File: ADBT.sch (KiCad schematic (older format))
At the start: 99 parts, among them J1 ADB1, J2 microUSB, Q1 AO3401, Q2 MMBT3904, Q3 MMBT3904, Q4 MMBT3904, Q5 MMBT3904, SW1 SW_Push, SW2 SW_Push, U1 ESP-WROOM-32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

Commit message: Add ground connection to LPseries mounting holes in schematic
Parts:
- H1, H2, H3, H4: symbol Mechanical:MountingHole -> Mechanical:MountingHole_Pad
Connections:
- net GND: now also H1.1, H2.1, H3.1, H4.1
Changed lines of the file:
@@
 encoding utf-8
 Sheet 1 1
-Title "RAM2E II"
-Date "2020-07-25"
-Rev "1.0"
+Title "ADBT"
+Date "2021-02-05"
+Rev "0.5"
 Comp "Garrett's Workshop"
 Comment1 ""
@@
 ESP32 module
 Wire Notes Line
-	2450 5850 1100 5850
-Text Notes 1250 5800 0    50   ~ 0
+	2450 5700 1100 5700
+Text Notes 1250 5650 0    50   ~ 0
 mounting holes & fiducials
 $Comp
@@
 	1100 6900 2450 6900
 Wire Notes Line
-	2450 5850 2450 6900
-Wire Notes Line
-	1100 5850 1100 6900
+	2450 5700 2450 6900
+Wire Notes Line
+	1100 5700 1100 6900
 Text Notes 2900 7100 0    50   ~ 0
 bypass capacitance
@@
 $EndComp
 $Comp
-L Mechanical:MountingHole H4
+L Mechanical:MountingHole_Pad H4
 U 1 1 5CC7E0C0
-P 2150 6000
-F 0 "H4" H 2250 6000 50  0000 L CNN
-F 1 " " H 2250 5960 50  0000 L CNN
-F 2 "stdpads:LPSeries-Screw" H 2150 6000 50  0001 C CNN
-F 3 "~" H 2150 6000 50  0001 C CNN
-	1    2150 6000
-	1    0    0    -1
-$EndComp
-$Comp
-L Mechanical:MountingHole H2
+P 2150 5900
+F 0 "H4" H 2250 5950 50  0000 L CNN
+F 1 " " H 2250 5860 50  0000 L CNN
+F 2 "stdpads:LPSeries-Screw" H 2150 5900 50  0001 C CNN
+F 3 "~" H 2150 5900 50  0001 C CNN
+	1    2150 5900
+	1    0    0    -1
+$EndComp
+$Comp
+L Mechanical:MountingHole_Pad H2
 U 1 1 5CC795A2
-P 1550 6000
-F 0 "H2" H 1650 6000 50  0000 L CNN
-F 1 " " H 1650 5960 50  0000 L CNN
-F 2 "stdpads:LPSeries-Screw" H 1550 6000 50  0001 C CNN
-F 3 "~" H 1550 6000 50  0001 C CNN
-	1    1550 6000
-	1    0    0    -1
-$EndComp
-$Comp
-L Mechanical:MountingHole H1
+P 1550 5900
+F 0 "H2" H 1650 5950 50  0000 L CNN
+F 1 " " H 1650 5860 50  0000 L CNN
+F 2 "stdpads:LPSeries-Screw" H 1550 5900 50  0001 C CNN
+F 3 "~" H 1550 5900 50  0001 C CNN
+	1    1550 5900
+	1    0    0    -1
+$EndComp
+$Comp
+L Mechanical:MountingHole_Pad H1
 U 1 1 5CC53461
-P 1250 6000
-F 0 "H1" H 1350 6000 50  0000 L CNN
-F 1 " " H 1350 5960 50  0000 L CNN
-F 2 "stdpads:LPSeries-Screw" H 1250 6000 50  0001 C CNN
-F 3 "~" H 1250 6000 50  0001 C CNN
-	1    1250 6000
-	1    0    0    -1
-$EndComp
-$Comp
-L Mechanical:MountingHole H3
+P 1250 5900
+F 0 "H1" H 1350 5950 50  0000 L CNN
+F 1 " " H 1350 5860 50  0000 L CNN
+F 2 "stdpads:LPSeries-Screw" H 1250 5900 50  0001 C CNN
+F 3 "~" H 1250 5900 50  0001 C CNN
+	1    1250 5900
+	1    0    0    -1
+$EndComp
+$Comp
+L Mechanical:MountingHole_Pad H3
 U 1 1 5CC7E0B9
-P 1850 6000
-F 0 "H3" H 1950 6000 50  0000 L CNN
-F 1 " " H 1950 5960 50  0000 L CNN
-F 2 "stdpads:LPSeries-Screw" H 1850 6000 50  0001 C CNN
-F 3 "~" H 1850 6000 50  0001 C CNN
-	1    1850 6000
+P 1850 5900
+F 0 "H3" H 1950 5950 50  0000 L CNN
+F 1 " " H 1950 5860 50  0000 L CNN
+F 2 "stdpads:LPSeries-Screw" H 1850 5900 50  0001 C CNN
+F 3 "~" H 1850 5900 50  0001 C CNN
+	1    1850 5900
 	1    0    0    -1
 $EndComp
@@
 $EndComp
 Connection ~ 900  1150
+Wire Wire Line
+	2150 6000 1850 6000
+Connection ~ 2150 6000
+Connection ~ 1550 6000
+Wire Wire Line
+	1550 6000 1250 6000
+Connection ~ 1850 6000
+Wire Wire Line
+	1850 6000 1550 6000
+Wire Wire Line
+	2150 6000 2250 5950
+$Comp
+L power:GND #PWR?
+U 1 1 602195C0
+P 2250 5950
+F 0 "#PWR?" H 2250 5700 50  0001 C CNN
+F 1 "GND" H 2250 5800 50  0000 C CNN
+F 2 "" H 2250 5950 50  0001 C CNN
+F 3 "" H 2250 5950 50  0001 C CNN
+	1    2250 5950
+	-1   0    0    -1
+$EndComp
 $EndSCHEMATC

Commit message: Switch to MLCC caps
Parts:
- removed C1, C2: 470u, stdpads:CP_Elec_10mm, symbol Device:CP_Small
- removed C27: 2u2, stdpads:C_0603, symbol Device:C_Small
- removed R18: 1k, stdpads:R_0603, symbol Device:R_Small
- removed SW2: SW_Push, stdpads:XKB_TS-1187A, symbol Switch:SW_Push
- added C1, C2: 100u, stdpads:C_1210, symbol Device:C_Small
- C11: value 100n -> 100u; footprint stdpads:C_0603 -> stdpads:C_1210
- C25, C26: value 2u2 -> 100u; footprint stdpads:C_0603 -> stdpads:C_1210
- R4: value 3k3 -> 1k
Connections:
- net +3V3: now also C11.1, C2.1
- net +5V: now also C1.1; no longer C11.1
- net BLED: now also U1.31 (IO19)
- net BTN0: now also U1.33 (IO21)
- net GLED: now also U1.30 (IO18)
- net GND: now also C11.2, C1.2, C2.2; no longer R4.2
- net RLED: now also U1.29 (IO5)
- net at D2.2 (A), F2.2, R2.2: now also R4.1
- net at C12.1, D6.1 (K), Q1.1 (G)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: no longer C11.2, R4.1
- no-connect marks 15 -> 18
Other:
- moved on the sheet: C18, C19, C20, C21, C22, C23, C24, R4

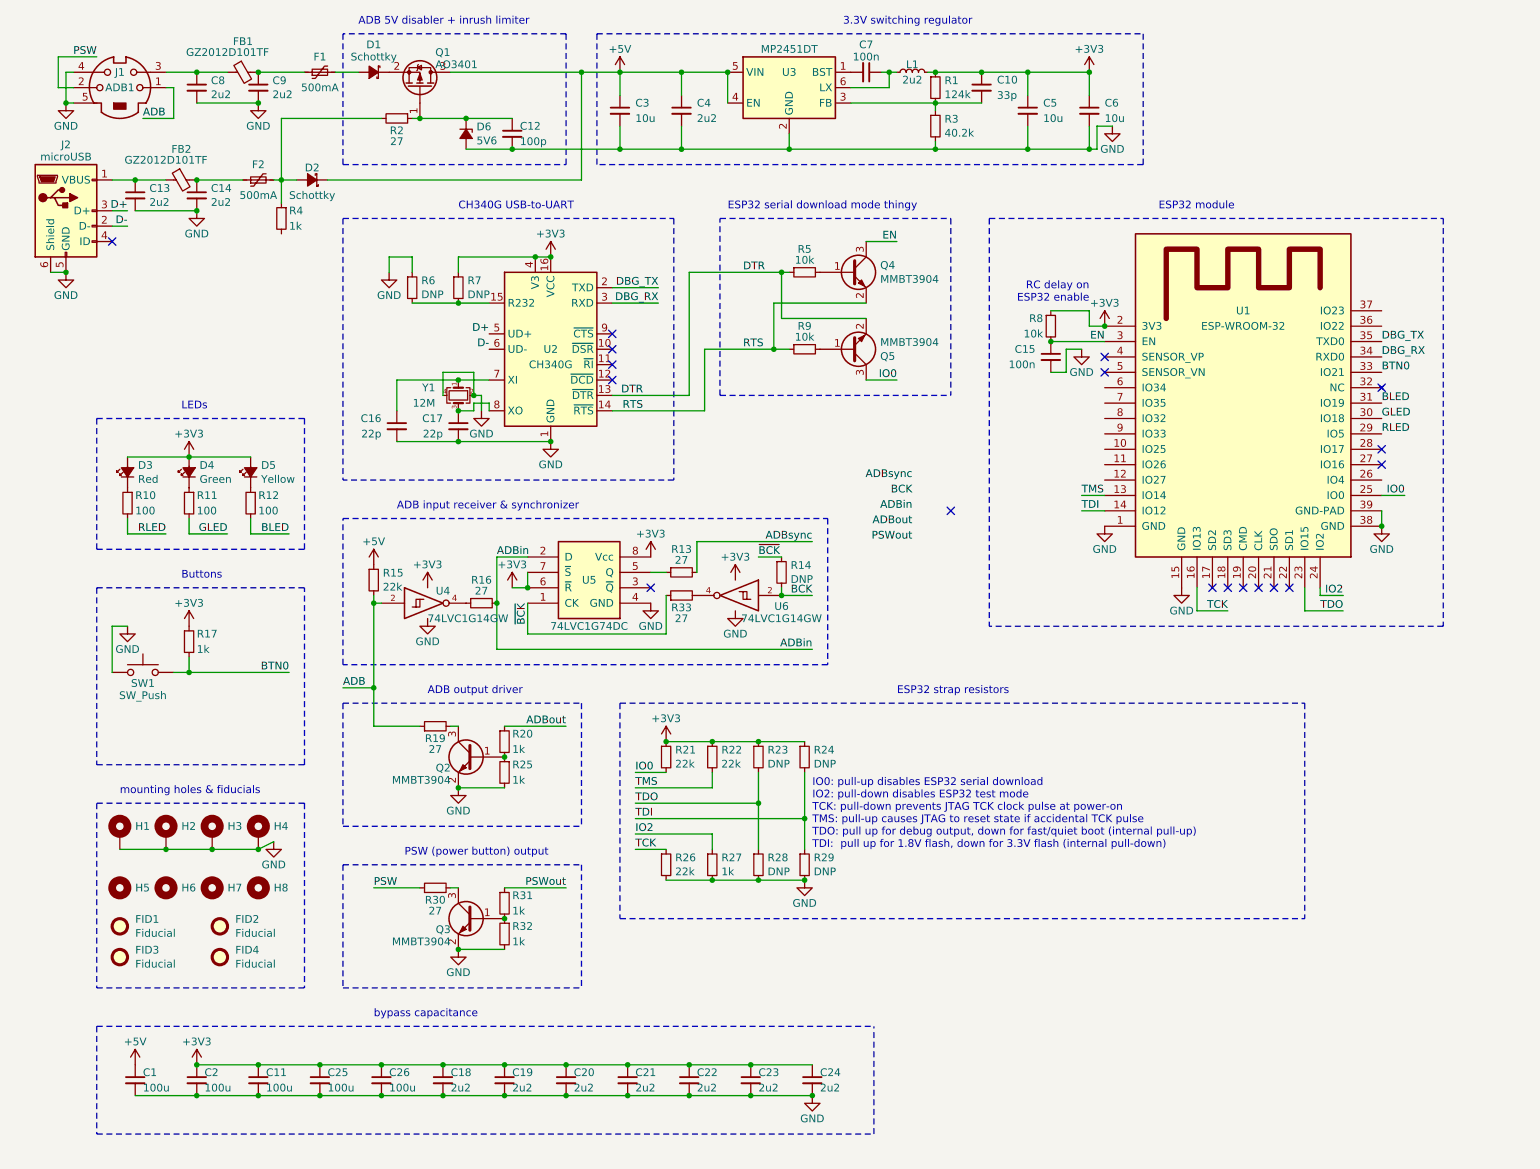
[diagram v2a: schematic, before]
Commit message: Lay out most of board
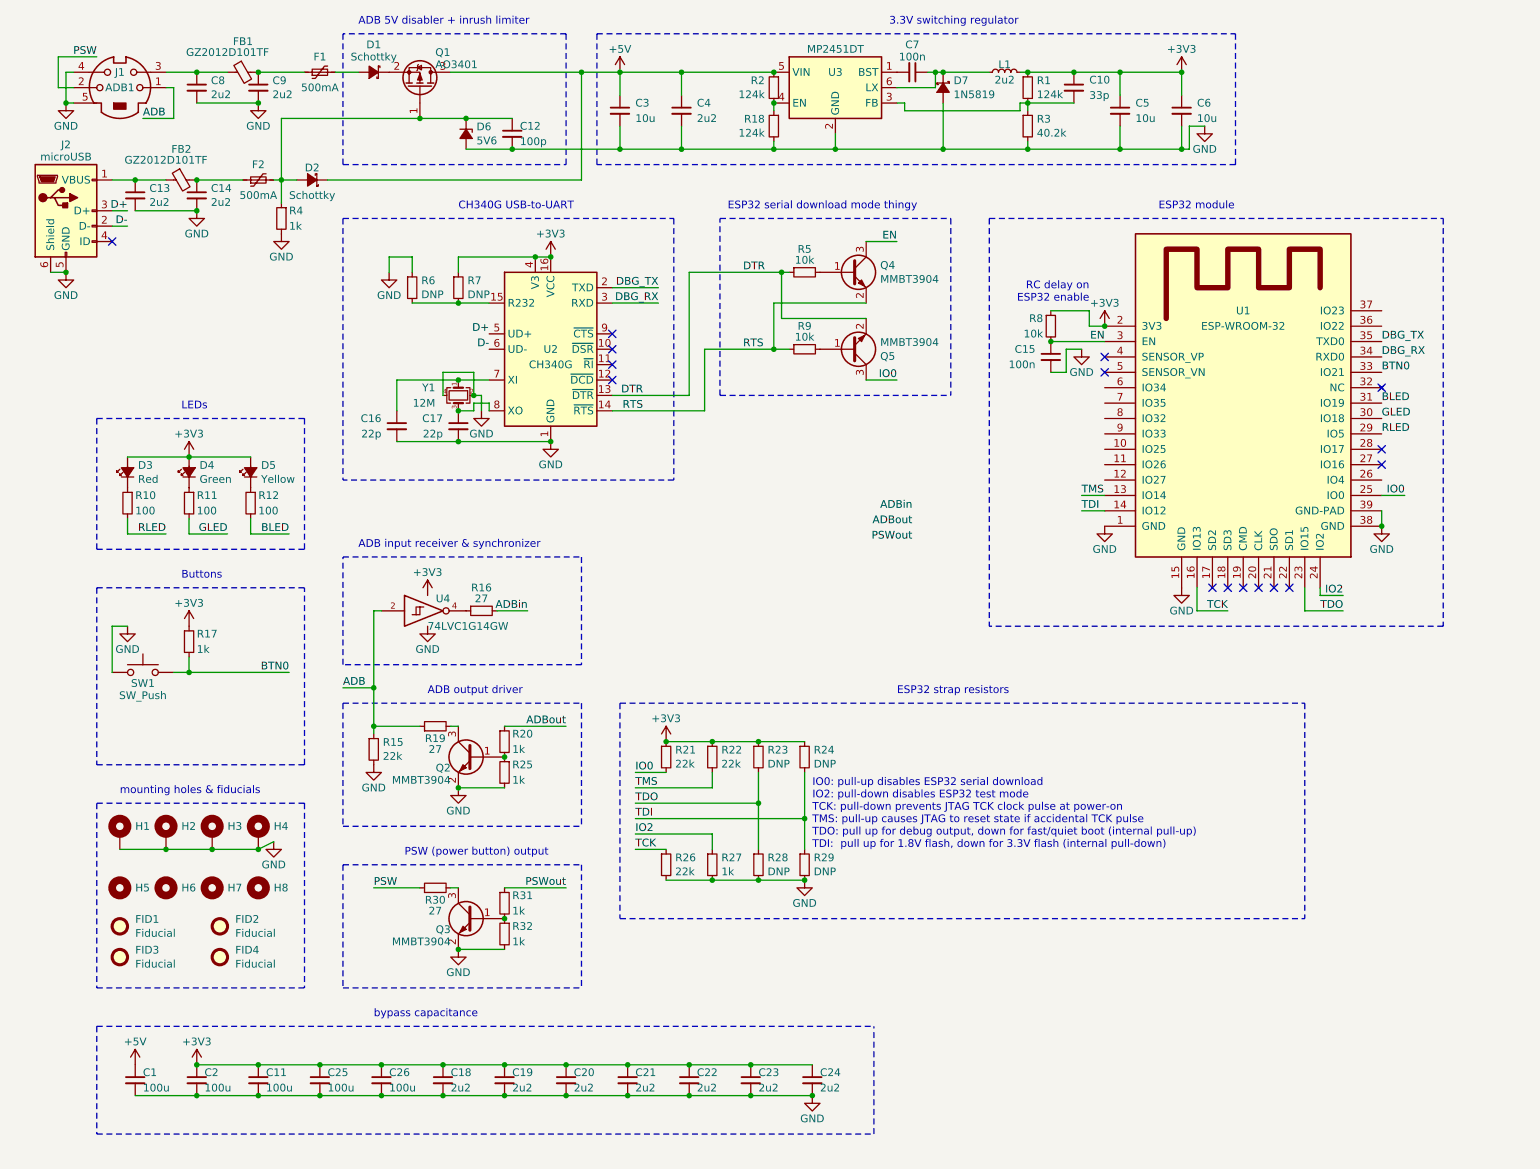
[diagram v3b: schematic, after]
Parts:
- removed R13, R33: 27, stdpads:R_0603, symbol Device:R_Small
- removed R14: DNP, stdpads:R_0603, symbol Device:R_Small
- removed U5: 74LVC1G74DC, stdpads:NXP_VSSOP-8_2.3x2mm, symbol GW_Logic:741G74DC
- removed U6: 74LVC1G14GW, stdpads:SOT-353, symbol 74xGxx:74LVC1G14
- added D7: 1N5819, stdpads:D_SOD-123, symbol Device:D_Schottky_Small_ALT
- added R18: 124k, stdpads:R_0603, symbol Device:R_Small
- R2: value 27 -> 124k
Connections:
- net +5V: now also R2.1; no longer R15.1, U3.4 (EN)
- net ADB: now also R15.1; no longer R15.2
- net GND: now also R15.2, R4.2, D7.2 (A), R18.2
- net at C7.1, L1.1, U3.6 (LX): now also D7.1 (K)
- net at D2.2 (A), F2.2, R4.1: now also C12.1, D6.1 (K), Q1.1 (G); no longer R2.2
- new net: R18.1, R2.2, U3.4 (EN)
- no-connect marks 18 -> 16
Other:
- moved on the sheet: C10, C5, C6, C7, L1, R1, R15, R16, R3, U3, U4

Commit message: Stitch board around edges
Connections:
- net at C16.1, U2.7 (XI): now also Y1.3; no longer Y1.1
- net at C17.1, U2.8 (XO): now also Y1.1; no longer Y1.3
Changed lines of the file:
@@
 	1    0    0    -1
 $EndComp
-Text Notes 3250 5000 0    50   ~ 0
+Text Notes 3150 5000 0    50   ~ 0
 ADB output driver
 $Comp
@@
 F 4 "C9002" H 3450 3050 50  0001 C CNN "LCSC Part"
 	1    3450 3050
-	0    -1   1    0
+	0    -1   -1   0
 $EndComp
 Connection ~ 3450 2950
@@
 Text Label 9450 3300 0    50   ~ 0
 RLED
-Text Label 6400 3800 2    50   ~ 0
+Text Label 6150 3350 2    50   ~ 0
 ADBin
-Text Label 6400 3900 2    50   ~ 0
+Text Label 6150 3450 2    50   ~ 0
 ADBout
-Text Label 6400 4000 2    50   ~ 0
+Text Label 6150 3550 2    50   ~ 0
 PSWout
 Wire Wire Line

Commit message: Layout done?
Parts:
- added C27, C28: 100u, stdpads:C_1210, symbol Device:C_Small
- added C29: 2u2, stdpads:C_0603, symbol Device:C_Small
- added R13: 1k, stdpads:R_0603, symbol Device:R_Small
- added SW2: SW_Push, stdpads:XKB_TS-1187A, symbol Switch:SW_Push
- U1: footprint stdpads:ESP32-WROVER_WROOM-32 -> stdpads:ESP32-WROVER_WROOM-32_WROOM
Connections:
- net +3V3: now also C27.1, C28.1, C29.1, R13.1
- net ADBin: now also U1.7 (IO35)
- net ADBout: now also U1.8 (IO32)
- net GND: now also C27.2, C28.2, C29.2, SW2.2
- net PSWout: now also U1.9 (IO33)
- net BTN1: now reaches U1.6 (IO34)
- net BTN1: now also R13.2, SW2.1
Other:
- moved on the sheet: C1, C10, C11, C18, C19, C2, C20, C21, C22, C23, C24, C25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

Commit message: Fabbed
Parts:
- removed D1: Schottky, stdpads:D_SMA, symbol Device:D_Schottky_Small_ALT
- added C30, C32, C33: 2u2, stdpads:C_0603, symbol Device:C_Small
- added C31: 10u, stdpads:C_0805, symbol Device:C_Small
- added FID5: Fiducial, stdpads:Fiducial, symbol Mechanical:Fiducial
- added J3: JTAG, stdpads:Tag-Connect_TC2050-IDC-NL_2x05_P1.27mm_Vertical, symbol Connector_Generic:Conn_02x05_Counter_Clockwise
- added Q6: AO3401, stdpads:SOT-23, symbol Device:Q_PMOS_GSD
- added R14, R34: 27, stdpads:R_0603, symbol Device:R_Small
- added R33: DNP, stdpads:R_0603, symbol Device:R_Small
- added R35: 1k, stdpads:R_0603, symbol Device:R_Small
- C1, C11, C2, C25, C26, C27, C28: LCSC Part (none) -> C49066
- C10: LCSC Part (none) -> C1663
- C12: value 100p -> 2u2; LCSC Part (none) -> C23630
- C13, C14, C18, C19, C20, C21, C22, C23, C24, C29, C4, C8, C9: LCSC Part (none) -> C23630
- C15, C7: LCSC Part (none) -> C14663
- C16, C17: LCSC Part (none) -> C1653
- C3, C5, C6: LCSC Part (none) -> C15850
- D2: value Schottky -> SS54
- D3: renamed from D4; footprint LED_SMD:LED_0805_2012Metric -> stdpads:LED_0805
- D4: renamed from D5; footprint LED_SMD:LED_0805_2012Metric -> stdpads:LED_0805
- D5: renamed from D3; footprint LED_SMD:LED_0805_2012Metric -> stdpads:LED_0805
- D7: LCSC Part (none) -> C8598
- F1, F2: value 500mA -> 1A; LCSC Part C69688 -> C66453
- L1: value 2u2 -> 4u7; LCSC Part C408335 -> C408337
- R1: value 124k -> 120k; LCSC Part (none) -> C25808
- R10, R11, R12: LCSC Part (none) -> C22775
- R13, R17, R20, R25, R27, R31, R32, R4: LCSC Part (none) -> C21190
- R15: value 22k -> 1M; LCSC Part (none) -> C22935
- R16, R19, R30: LCSC Part (none) -> C25190
- R18, R2: value 124k -> 1k; LCSC Part (none) -> C21190
- R21, R22, R26: LCSC Part (none) -> C31850
- R3: value 40.2k -> 39k; LCSC Part (none) -> C23153
- R5, R8, R9: LCSC Part (none) -> C25804
- R6: value DNP -> 1k; LCSC Part (none) -> C21190
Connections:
- net BLED is gone; now on net RLED: R12.2, U1.31 (IO19)
- net +3V3: now also C12.1, C30.1, C32.1, C33.1, J3.1 (Pin_1)
- net +5V: now also C31.1, Q6.2 (S); no longer Q1.3 (D)
- net EN: now also R33.2, R34.2
- net GLED: now also R10.2, U1.29 (IO5); no longer R11.2, U1.30 (IO18)
- net GND: now also R6.2, C30.2, C31.2, C32.2, C33.2, J3.3 (Pin_3), R35.2; no longer R6.1
- net RLED: no longer R10.2, U1.29 (IO5)
- net TCK: now also R14.1
- net TDI: now also J3.8 (Pin_8)
- net TDO: now also J3.6 (Pin_6)
- net TMS: now also J3.2 (Pin_2)
- net at D2.2 (A), D6.1 (K), F2.2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: now also Q6.1 (G); no longer C12.1
- net at R7.2, U2.15 (R232): now also R6.1; no longer R6.2
- net at Q1.2 (S): now also F1.2, R35.1
- net at D5.1 (K): now also R12.1; no longer R10.1
- net at D3.1 (K): now also R10.1; no longer R11.1
- net at D4.1 (K): now also R11.1; no longer R12.1
- new net: J3.4 (Pin_4), R14.2
- new net: Q1.3 (D), Q6.3 (D)
- new net YLED: R11.2, U1.30 (IO18)
- new net ~SRST~: J3.10 (Pin_10), R34.1
- new net ~TRST~: J3.9 (Pin_9), R33.1
- no-connect marks 16 -> 18
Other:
- note added: "ADB 5V disabler"
- note added: "ADB input receiver"
- note removed: "ADB 5V disabler + inrush limiter"
- note removed: "ADB input receiver & synchronizer"
- moved on the sheet: C1, C10, C11, C13, C14, C15, C18, C19, C2, C20, C21, C22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
